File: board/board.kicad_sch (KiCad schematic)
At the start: 14 parts, among them J1 Conn_01x05, P1 USB_C_Plug_USB2.0, U1 FT232RL

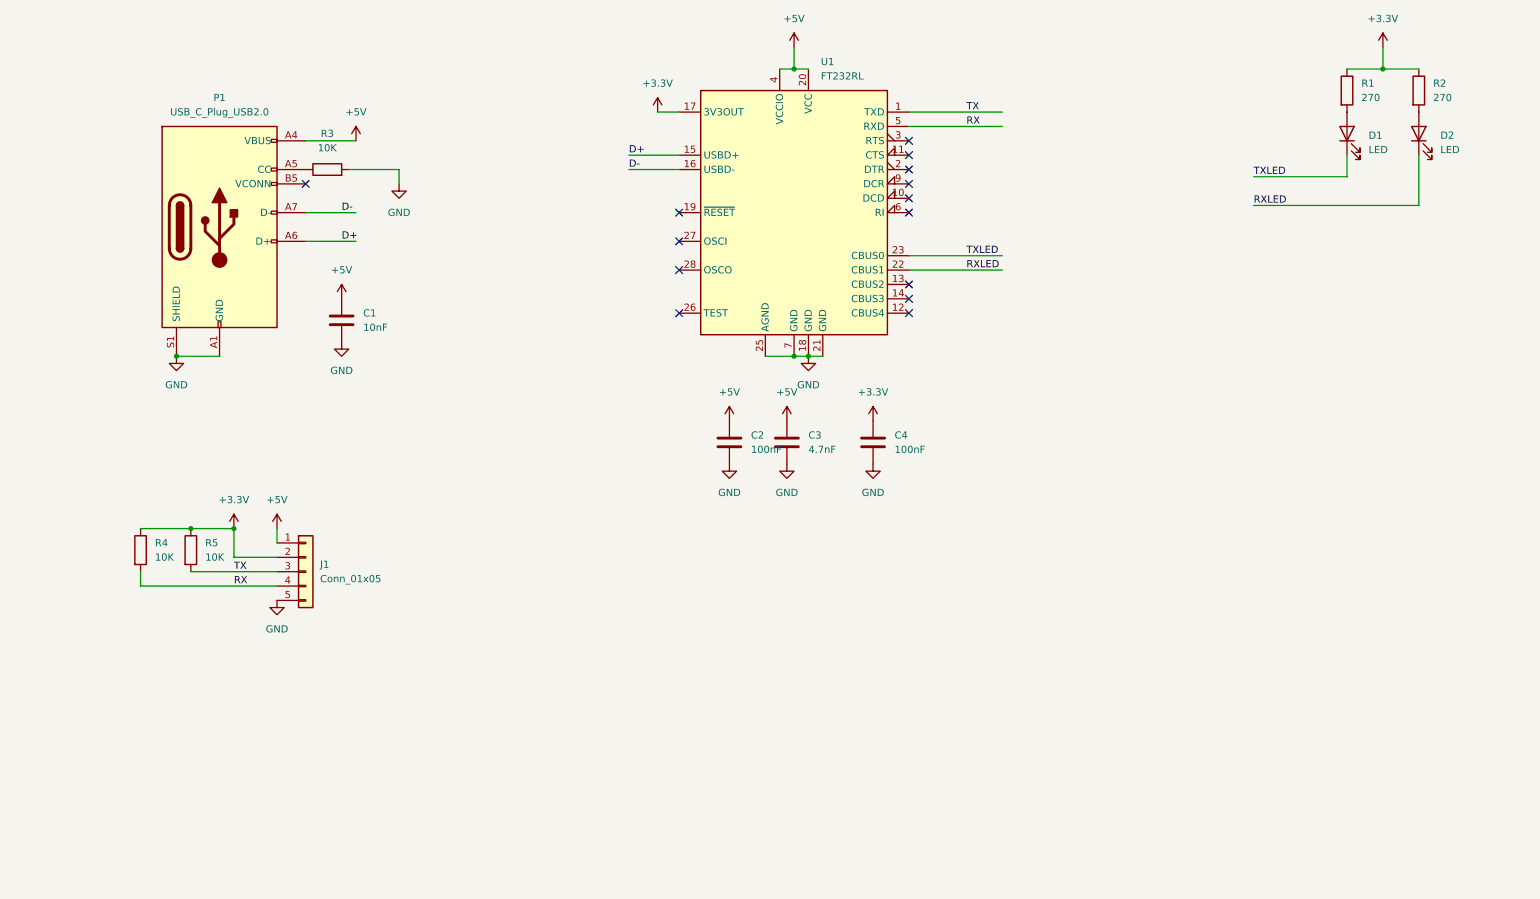
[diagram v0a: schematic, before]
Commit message: feat(bsp/usb-ttl/debug): schematic
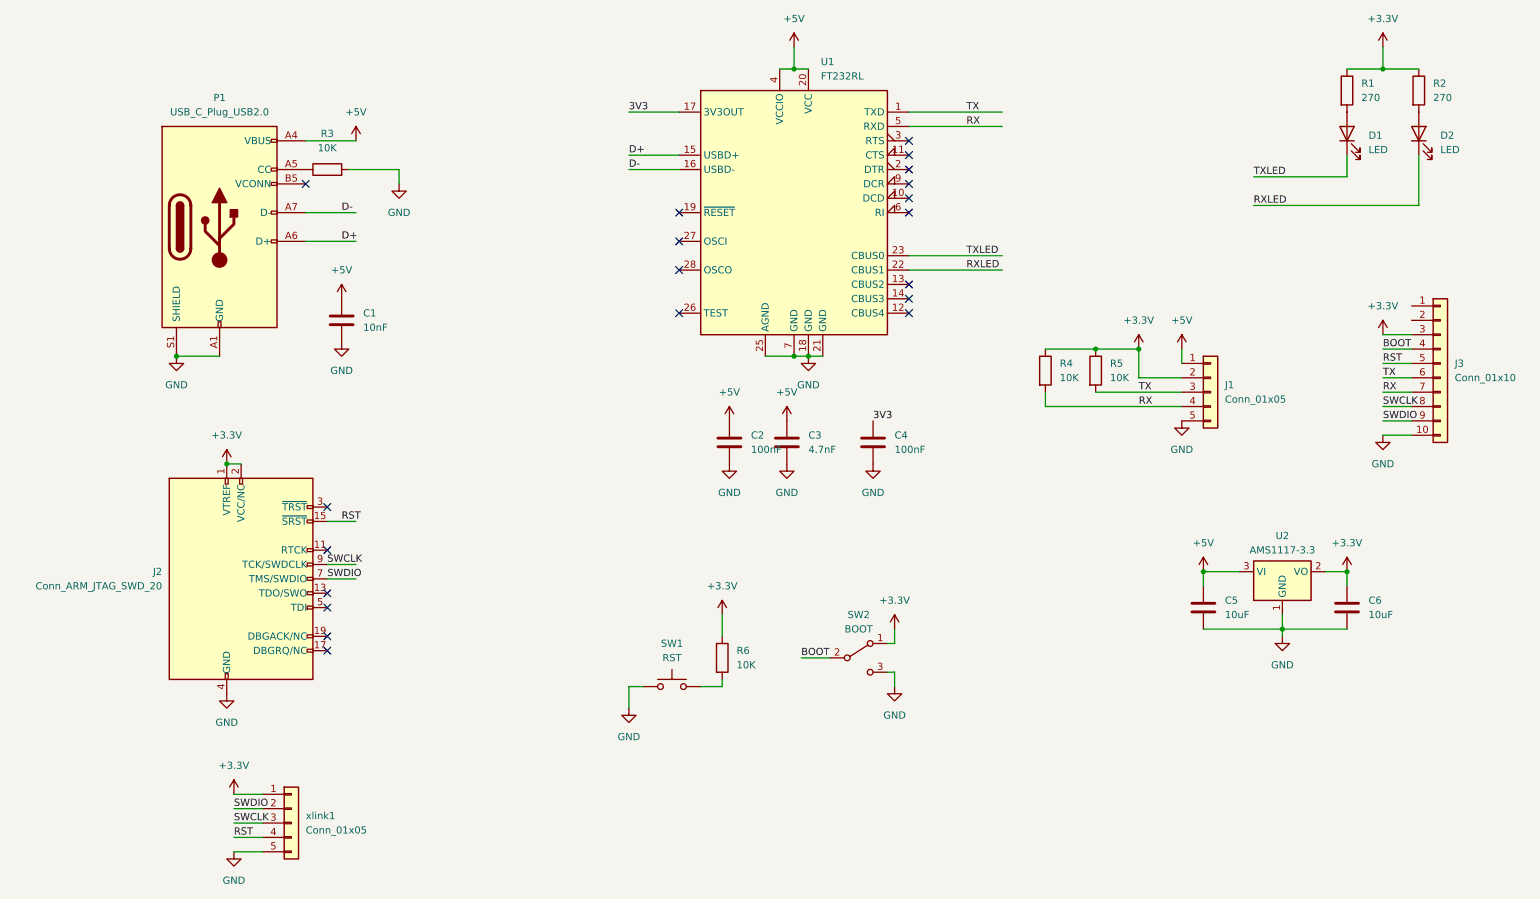
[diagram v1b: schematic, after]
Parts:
- added C5, C6: 10uF, Capacitor_SMD:C_0402_1005Metric_Pad0.74x0.62mm_HandSolder, symbol Device:C
- added J2: Conn_ARM_JTAG_SWD_20, Connector_IDC:IDC-Header_2x10_P2.54mm_Vertical, symbol Connector:Conn_ARM_JTAG_SWD_20
- added J3: Conn_01x10, Connector_FFC-FPC:Molex_54548-1071_1x10-1MP_P0.5mm_Horizontal, symbol Connector_Generic:Conn_01x10
- added R6: 10K, Resistor_SMD:R_0402_1005Metric_Pad0.72x0.64mm_HandSolder, symbol Device:R
- added SW1: RST, Button_Switch_SMD:SW_SPST_Omron_B3FS-100xP, symbol Switch:SW_Push
- added SW2: BOOT, Button_Switch_SMD:SW_SPDT_CK-JS102011SAQN, symbol Switch:SW_SPDT
- added U2: AMS1117-3.3, Package_TO_SOT_SMD:SOT-223-3_TabPin2, symbol Regulator_Linear:AMS1117-3.3
- added xlink1: Conn_01x05, Connector_PinHeader_2.54mm:PinHeader_1x05_P2.54mm_Vertical, symbol Connector_Generic:Conn_01x05
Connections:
- net +3.3V: now also C6.1, J2.1 (VTREF), J2.2 (VCC/NC), J3.3 (Pin_3), R6.1, SW2.1 (A), U2.2 (VO), xlink1.1 (Pin_1); no longer C4.1, U1.17 (3V3OUT)
- net +5V: now also C5.1, U2.3 (VI)
- net GND: now also C5.2, C6.2, J2.10 (GND), J2.12 (GND), J2.14 (GND), J2.16 (GND), J2.18 (GND), J2.20 (GND), J2.4 (GND), J2.6 (GND), J2.8 (GND), J3.10 (Pin_10), SW1.1, SW2.3 (C), U2.1 (GND), xlink1.5 (Pin_5)
- net RX: now also J3.7 (Pin_7)
- net TX: now also J3.6 (Pin_6)
- new net: R6.2, SW1.2
- new net 3V3: C4.1, U1.17 (3V3OUT)
- new net BOOT: J3.4 (Pin_4), SW2.2 (B)
- new net RST: J2.15 (~{SRST}), J3.5 (Pin_5), xlink1.4 (Pin_4)
- new net SWCLK: J2.9 (TCK/SWDCLK), J3.8 (Pin_8), xlink1.3 (Pin_3)
- new net SWDIO: J2.7 (TMS/SWDIO), J3.9 (Pin_9), xlink1.2 (Pin_2)
- no-connect marks 14 -> 20
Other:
- moved on the sheet: J1, R4, R5

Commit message: feat(bsp/usb-ttl/debug): pcb layer
aa
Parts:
- renumbered SW1 to RST1
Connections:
- net +3.3V: now also J3.1 (Pin_1); no longer J3.3 (Pin_3)
- net BOOT: now also J3.9 (Pin_9); no longer J3.4 (Pin_4)
- net RST: now also J3.8 (Pin_8), R6.2, RST1.2; no longer J3.5 (Pin_5)
- net SWCLK: now also J3.2 (Pin_2); no longer J3.8 (Pin_8)
- net SWDIO: now also J3.3 (Pin_3); no longer J3.9 (Pin_9)
- no-connect marks 20 -> 22
